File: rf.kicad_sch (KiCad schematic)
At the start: 13 parts

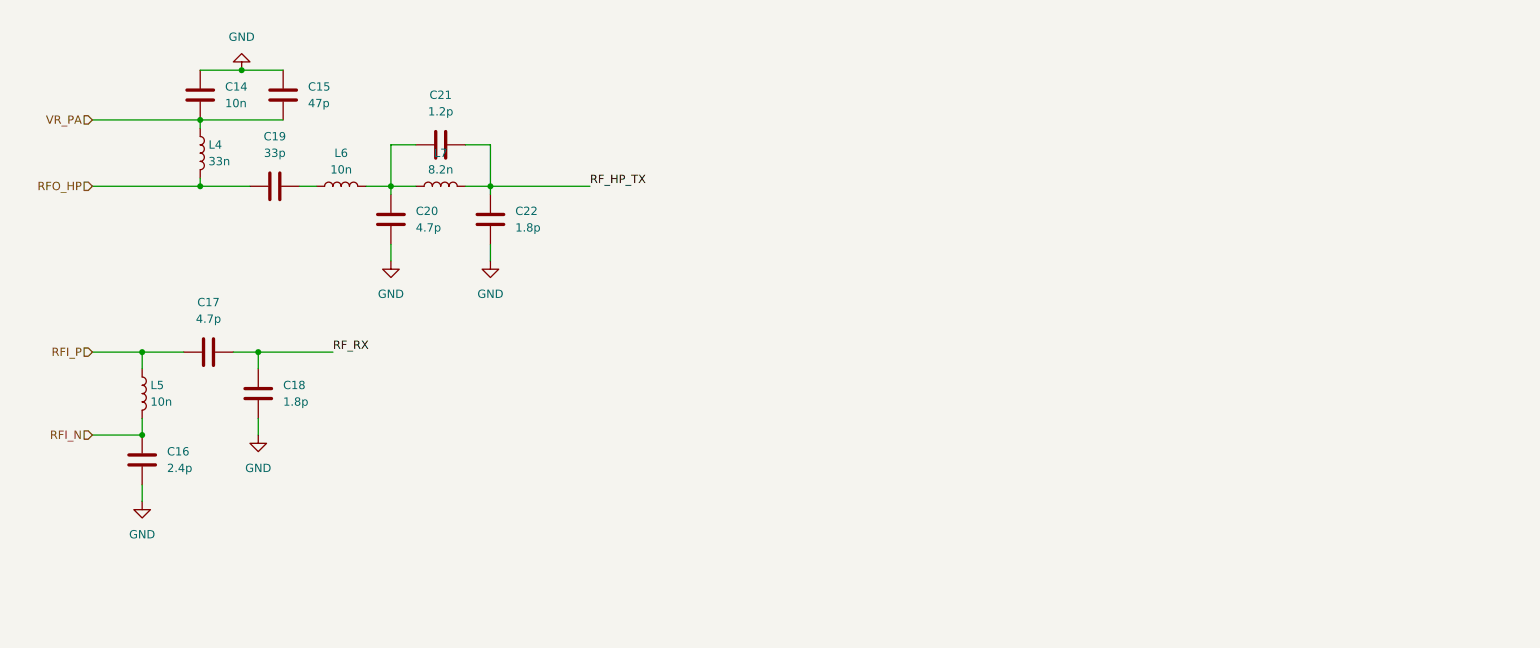
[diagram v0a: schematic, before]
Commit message: Finished schematic v1, start PCB
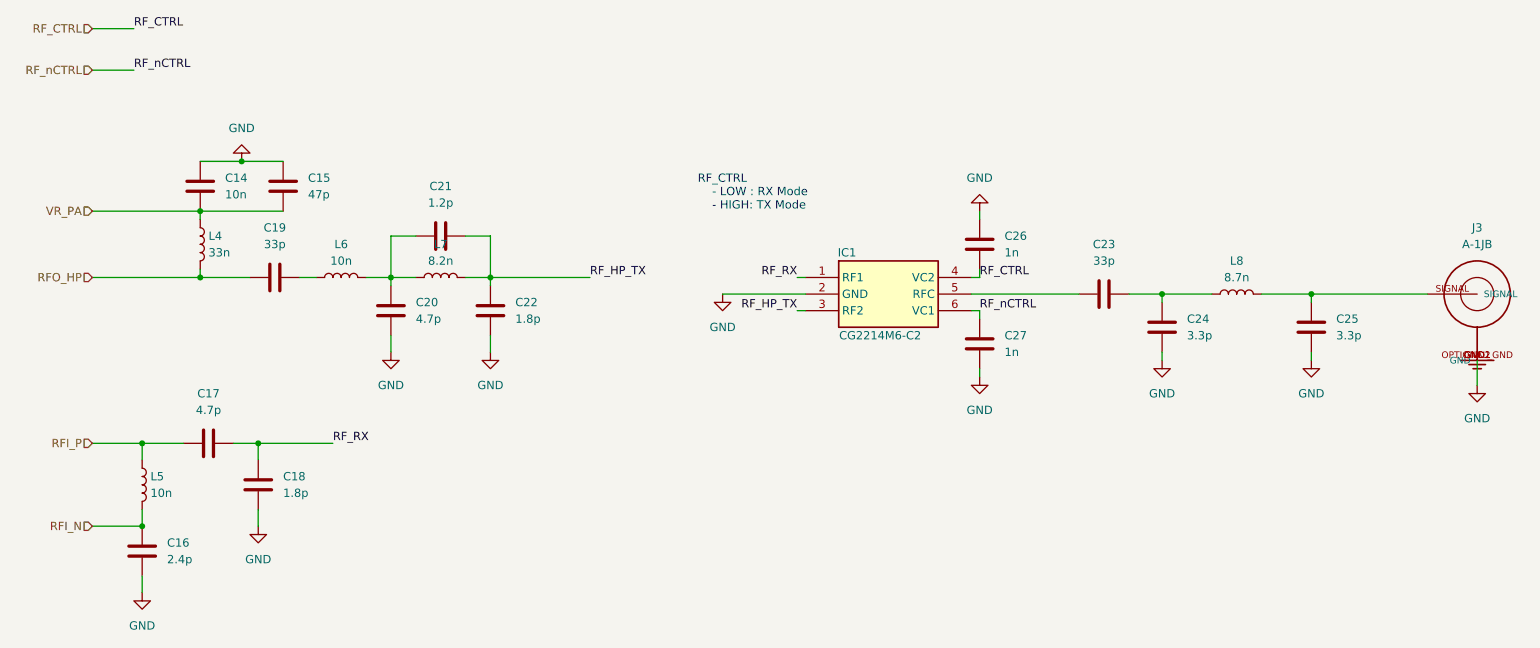
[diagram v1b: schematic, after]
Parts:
- added C23: 33p, Capacitor_SMD:C_0603_1608Metric, symbol Device:C
- added C24, C25: 3.3p, Capacitor_SMD:C_0603_1608Metric, symbol Device:C
- added C26, C27: 1n, Capacitor_SMD:C_0603_1608Metric, symbol Device:C
- added IC1: CG2214M6-C2, CG2214M6-C2:SOTFL48P130X55-6N, symbol CG2214M6-C2:CG2214M6-C2
- added J3: A-1JB, A-1JB:AMPHENOL_A-1JB, symbol A-1JB:A-1JB
- added L8: 8.7n, Inductor_SMD:L_0603_1608Metric, symbol Device:L
- C14, C15, C16, C17, C18, C19, C20, C21, C22: footprint (none) -> Capacitor_SMD:C_0603_1608Metric
- L4, L5, L6, L7: footprint (none) -> Inductor_SMD:L_0603_1608Metric
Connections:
- net GND: now also C24.2, C25.2, C26.2, C27.1, IC1.2 (GND), J3.GND1 (GND), J3.GND2 (GND), J3.OPTIONAL_GND (GND)
- net RF_HP_TX: now also IC1.3 (RF2)
- net RF_RX: now also IC1.1 (RF1)
- new net: C25.1, J3.SIGNAL, L8.2
- new net: C23.2, C24.1, L8.1
- new net: C23.1, IC1.5 (RFC)
- new net RF_CTRL: C26.1, IC1.4 (VC2)
- new net RF_nCTRL: C27.2, IC1.6 (VC1)
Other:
- note added: "RF_CTRL - LOW : RX Mode - HIGH: TX Mode"
- moved on the sheet: C14, C15, C16, C17, C18, C19, C20, C21, C22, L4, L5, L6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
